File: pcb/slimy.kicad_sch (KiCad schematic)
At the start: 3 parts, among them U1 Teensy3.2, U2 PIM447

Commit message: WIP keyboard pcb design
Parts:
- removed U3: (no value), symbol my_lib:ST7789_240x240
- added D1, D10, D11, D12, D13, D14, D15, D16, D17, D18, D19, D2, D20, D21, D22, D23, D24, D25, D26, D27, D28, D29, D3, D30, D31, D32, D33, D34, D35, D36, D37, D38, D39, D4, D40, D41, D42, D43, D44, D45, D46, D47, D48, D49, D5, D50, D51, D52, D53, D54, D6, D7, D8, D9: D, my_lib:D_SOD123_axial, symbol kicad_lib_tmk:D
- added K1, K10, K11, K12, K13, K14, K15, K16, K17, K18, K19, K2, K20, K21, K22, K23, K24, K25, K26, K27, K28, K29, K3, K30, K31, K32, K33, K34, K35, K36, K37, K38, K39, K4, K40, K41, K42, K43, K44, K45, K46, K47, K48, K49, K5, K50, K51, K52, K53, K54, K6, K7, K8, K9: KEYSW, my_lib:MX-1U-Hotswap-Antishear, symbol kicad_lib_tmk:KEYSW
- added U3: ST7789_SPI, my_lib:ST7789_1.3_240x240, symbol my_lib:ST7789_SPI
- U1: renamed from U2; footprint (none) -> my_lib:PIM447
- U2: renamed from U1; footprint (none) -> teensy:Teensy30_31_32_All_Pins
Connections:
- net GND: now also U3.3 (GND)
- net LCD CS: now also U3.7 (TCS)
- net LCD DC: now also U3.9 (D/C)
- net LCD RST: now also U3.8 (RST)
- net VCC: now also U3.1 (Vin)
- net Col5: now reaches U2.10 (8_TX3_DIN)
- net Col5: now also K17.1, K29.1, K41.1, K5.1, K50.1
- net LCD LITE: now reaches U2.11 (9_RX2_CS_PWM)
- net LCD LITE: now also U3.11 (Lite)
- net Row4: now reaches U2.2 (0_RX1_Touch)
- net Row4: now also D37.1, D38.1, D39.1, D40.1, D41.1, D42.1, D43.1, D44.1, D45.1, D46.1, D47.1, D48.1
- net Row5: now reaches U2.21 (14_A0_SCK)
- net Row5: now also D49.1, D50.1, D51.1, D52.1, D53.1, D54.1, U3.4 (SCK)
- net Col12: now reaches U2.24 (17_A3_SDA0_Touch)
- net Col12: now also K12.1, K24.1, K36.1, K48.1
- net Col11: now reaches U2.27 (20_A6_CS_PWM)
- net Col11: now also K11.1, K23.1, K35.1, K47.1
- net Col10: now reaches U2.28 (21_A7_RX1_CS_PWM)
- net Col10: now also K10.1, K22.1, K34.1, K46.1
- net Col9: now reaches U2.29 (22_A8_Touch_PWM)
- net Col9: now also K21.1, K33.1, K45.1, K54.1, K9.1
- net Row3: now reaches U2.3 (1_TX1_Touch)
- net Row3: now also D25.1, D26.1, D27.1, D28.1, D29.1, D30.1, D31.1, D32.1, D33.1, D34.1, D35.1, D36.1
- net Col8: now reaches U2.30 (23_A9_Touch_PWM)
- net Col8: now also K20.1, K32.1, K44.1, K53.1, K8.1
- net Row2: now reaches U2.4 (2)
- net Row2: now also D13.1, D14.1, D15.1, D16.1, D17.1, D18.1, D19.1, D20.1, D21.1, D22.1, D23.1, D24.1
- net Row1: now reaches U2.5 (3_TX_PWM)
- net Row1: now also D1.1, D10.1, D11.1, D12.1, D2.1, D3.1, D4.1, D5.1, D6.1, D7.1, D8.1, D9.1
- net Col1: now reaches U2.6 (4_RX_PWM)
- net Col1: now also K1.1, K13.1, K25.1, K37.1
- net Col2: now reaches U2.7 (5_TX1_PWM)
- net Col2: now also K14.1, K2.1, K26.1, K38.1
- net Col3: now reaches U2.8 (6_PWM)
- net Col3: now also K15.1, K27.1, K3.1, K39.1
- net Col4: now reaches U2.9 (7_RX3_DOUT)
- net Col4: now also K16.1, K28.1, K4.1, K40.1, K49.1
- net MISO renamed Col7
- net Col7: now also K19.1, K31.1, K43.1, K52.1, K7.1
- net MOSI renamed Col6
- net Col6: now also K18.1, K30.1, K42.1, K51.1, K6.1, U3.6 (SI)
- net SCK: no longer names the net of U2.19 (A14/DAC)
- new net: D16.2, K16.2
- new net: D44.2, K44.2
- new net: D33.2, K33.2
- new net: D17.2, K17.2
- new net: D42.2, K42.2
- new net: D36.2, K36.2
- new net: D11.2, K11.2
- new net: D41.2, K41.2
- new net: D5.2, K5.2
- new net: D6.2, K6.2
- new net: D15.2, K15.2
- new net: D48.2, K48.2
- new net: D28.2, K28.2
- new net: D46.2, K46.2
- new net: D34.2, K34.2
- new net: D21.2, K21.2
- new net: D24.2, K24.2
- new net: D31.2, K31.2
- new net: D40.2, K40.2
- new net: D20.2, K20.2
- new net: D12.2, K12.2
- new net: D29.2, K29.2
- new net: D2.2, K2.2
- new net: D18.2, K18.2
- new net: D4.2, K4.2
- new net: D49.2, K49.2
- new net: D43.2, K43.2
- new net: D37.2, K37.2
- new net: D7.2, K7.2
- new net: D8.2, K8.2
- new net: D9.2, K9.2
- new net: D10.2, K10.2
- new net: D54.2, K54.2
- new net: D32.2, K32.2
- new net: D52.2, K52.2
- new net: D38.2, K38.2
- new net: D13.2, K13.2
- new net: D25.2, K25.2
- new net: D53.2, K53.2
- new net: D22.2, K22.2
- new net: D26.2, K26.2
- new net: D23.2, K23.2
- new net: D50.2, K50.2
- new net: D30.2, K30.2
- new net: D27.2, K27.2
- new net: D19.2, K19.2
- new net: D1.2, K1.2
- new net: D14.2, K14.2
- new net: D39.2, K39.2
- new net: D35.2, K35.2
- new net: D45.2, K45.2
- new net: D3.2, K3.2
- new net: D47.2, K47.2
- new net: D51.2, K51.2
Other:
- moved on the sheet: U1, U2

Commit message: First iteration design pt2
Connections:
- net Col1: no longer U2.6 (4_RX_PWM)
- net Col6: now also U2.6 (4_RX_PWM); no longer U2.13 (11_DOUT), U3.6 (SI)
- net Row1: now also U2.2 (0_RX1_Touch); no longer U2.5 (3_TX_PWM)
- net Row2: now also U2.3 (1_TX1_Touch); no longer U2.4 (2)
- net Row3: now also U2.4 (2); no longer U2.3 (1_TX1_Touch)
- net Row4: now also U2.5 (3_TX_PWM); no longer U2.2 (0_RX1_Touch)
- new net Col_: U2.13 (11_DOUT), U3.6 (SI)
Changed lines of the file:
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@@
     )
   )
-  (global_label "Row2" (shape input) (at 35.56 214.63 180) (fields_autoplaced)
+  (global_label "Row3" (shape input) (at 35.56 214.63 180) (fields_autoplaced)
     (effects (font (size 1.27 1.27)) (justify right))
     (property "Intersheet References" "${INTERSHEET_REFS}" (id 0) (at 28.1879 214.5506 0)
@@
     )
   )
-  (global_label "Row1" (shape input) (at 35.56 217.17 180) (fields_autoplaced)
+  (global_label "Row4" (shape input) (at 35.56 217.17 180) (fields_autoplaced)
     (effects (font (size 1.27 1.27)) (justify right))
     (property "Intersheet References" "${INTERSHEET_REFS}" (id 0) (at 28.1879 217.0906 0)
@@
     )
   )
-  (global_label "Row3" (shape input) (at 35.56 212.09 180) (fields_autoplaced)
+  (global_label "Row2" (shape input) (at 35.56 212.09 180) (fields_autoplaced)
     (effects (font (size 1.27 1.27)) (justify right))
     (property "Intersheet References" "${INTERSHEET_REFS}" (id 0) (at 28.1879 212.0106 0)
@@
     )
   )
-  (global_label "Col6" (shape input) (at 26.67 240.03 180) (fields_autoplaced)
-    (effects (font (size 1.27 1.27)) (justify right))
-    (property "Intersheet References" "${INTERSHEET_REFS}" (id 0) (at 19.9631 240.1094 0)
+  (global_label "Col_" (shape input) (at 26.67 240.03 180) (fields_autoplaced)
+    (effects (font (size 1.27 1.27)) (justify right))
+    (property "Intersheet References" "${INTERSHEET_REFS}" (id 0) (at 20.205 239.9506 0)
       (effects (font (size 1.27 1.27)) (justify right) hide)
     )
@@
     )
   )
-  (global_label "Col1" (shape input) (at 35.56 219.71 180) (fields_autoplaced)
+  (global_label "Col6" (shape input) (at 35.56 219.71 180) (fields_autoplaced)
     (effects (font (size 1.27 1.27)) (justify right))
     (property "Intersheet References" "${INTERSHEET_REFS}" (id 0) (at 28.8531 219.6306 0)
@@
     )
   )
-  (global_label "Row4" (shape input) (at 35.56 209.55 180) (fields_autoplaced)
+  (global_label "Row1" (shape input) (at 35.56 209.55 180) (fields_autoplaced)
     (effects (font (size 1.27 1.27)) (justify right))
     (property "Intersheet References" "${INTERSHEET_REFS}" (id 0) (at 28.1879 209.4706 0)

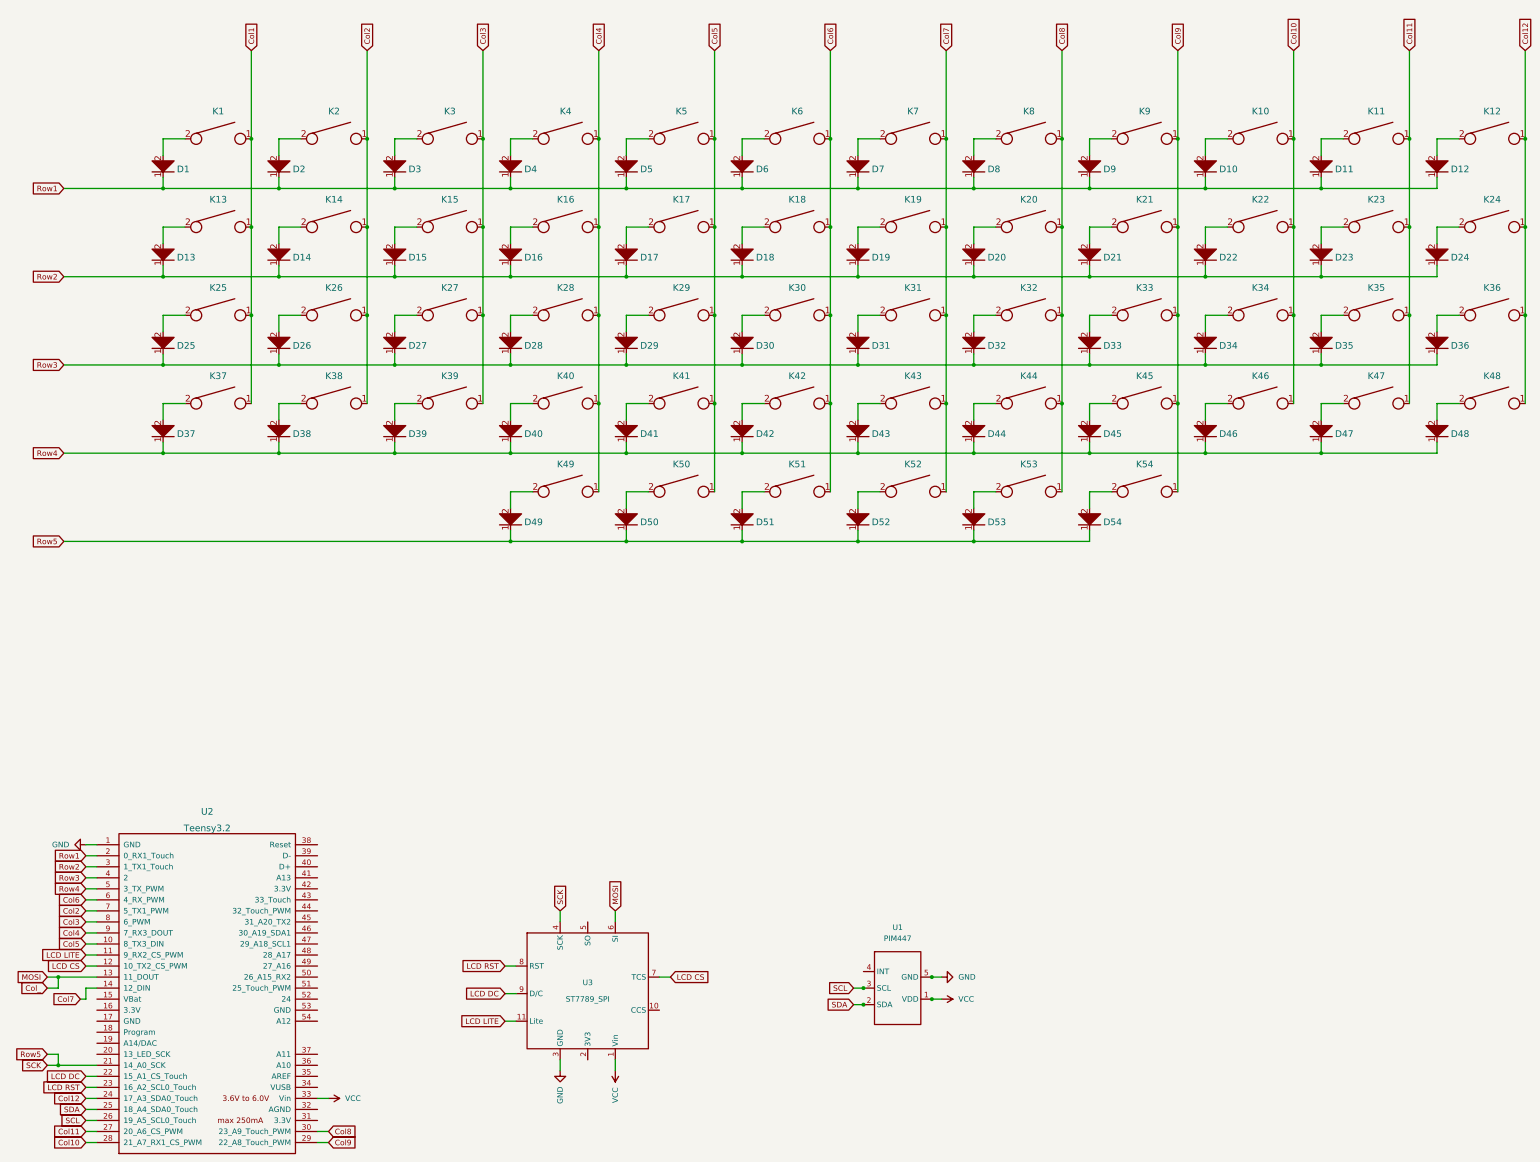
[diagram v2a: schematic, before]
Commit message: Wire everything switch related
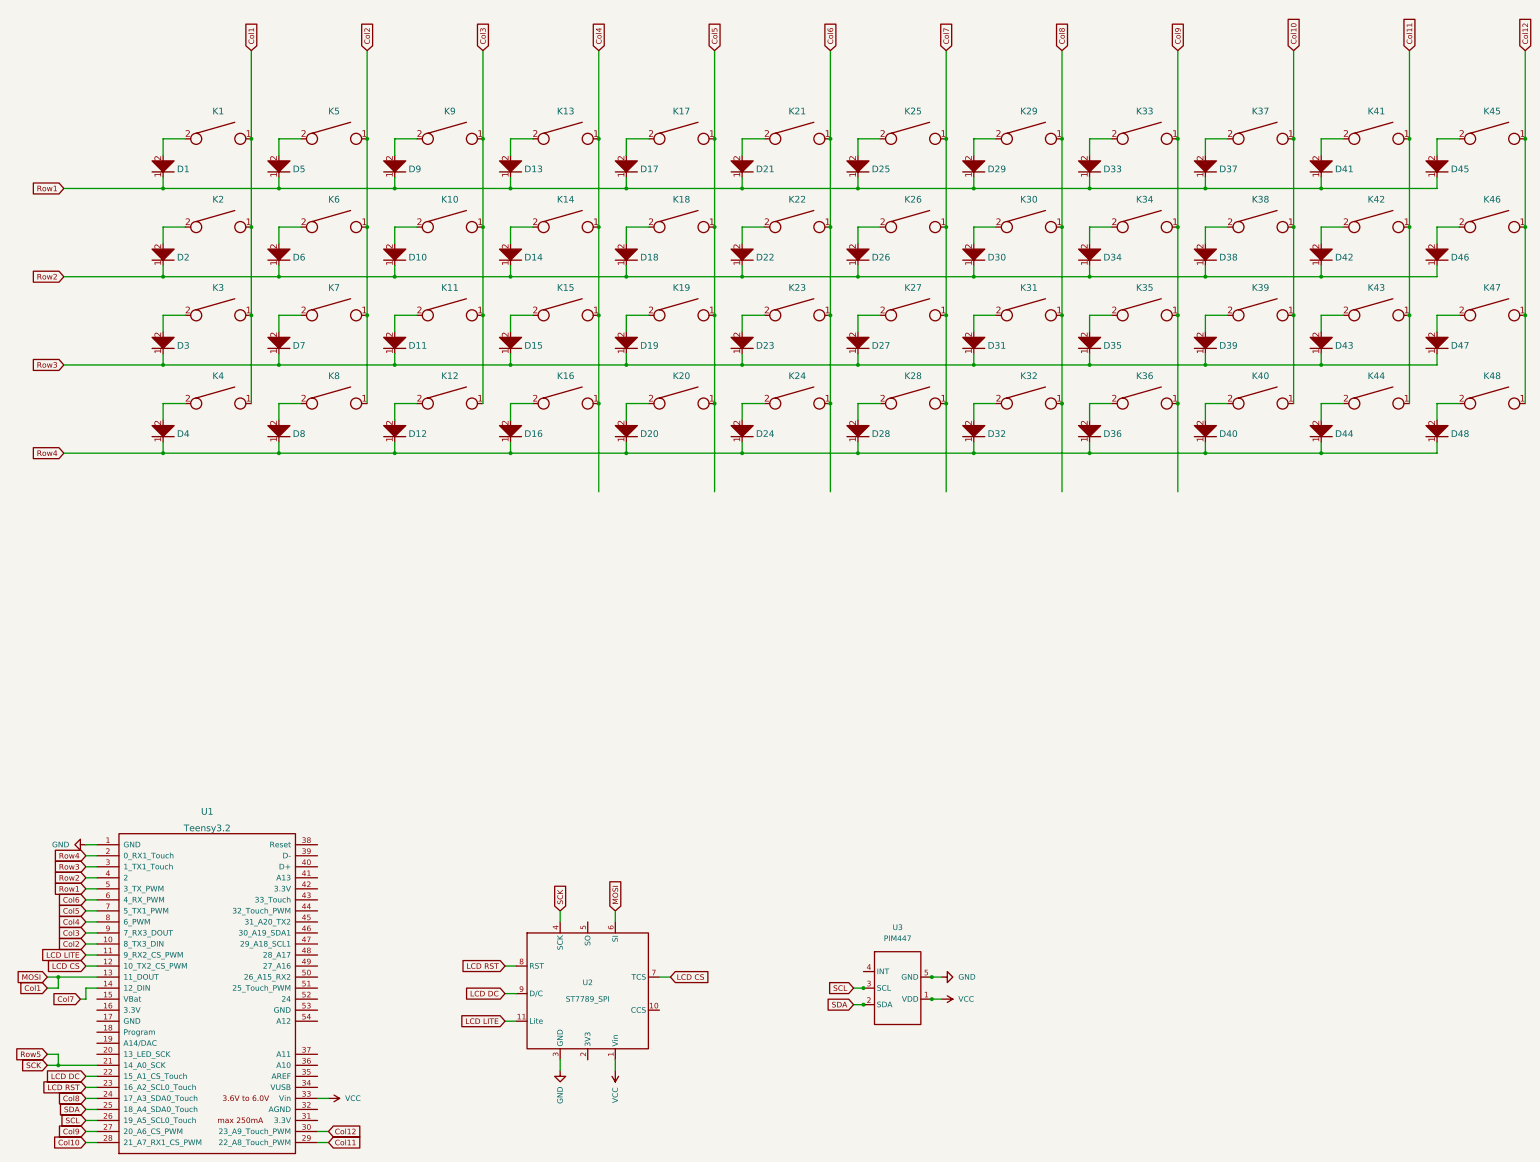
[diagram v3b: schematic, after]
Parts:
- removed D49, D50, D51, D52, D53, D54: D, my_lib:D_SOD123_axial, symbol kicad_lib_tmk:D
- removed K49, K50, K51, K52, K53, K54: KEYSW, my_lib:MX-1U-Hotswap-Antishear, symbol kicad_lib_tmk:KEYSW
- K1, K48: footprint my_lib:MX-1U-Hotswap-Antishear -> (none)
- K10: renamed from K15; footprint my_lib:MX-1U-Hotswap-Antishear -> (none)
- K11: renamed from K27; footprint my_lib:MX-1U-Hotswap-Antishear -> (none)
- K12: renamed from K39; footprint my_lib:MX-1U-Hotswap-Antishear -> (none)
- K13: renamed from K4; footprint my_lib:MX-1U-Hotswap-Antishear -> (none)
- K14: renamed from K16; footprint my_lib:MX-1U-Hotswap-Antishear -> (none)
- K15: renamed from K28; footprint my_lib:MX-1U-Hotswap-Antishear -> (none)
- K16: renamed from K40; footprint my_lib:MX-1U-Hotswap-Antishear -> (none)
- K17: renamed from K5; footprint my_lib:MX-1U-Hotswap-Antishear -> (none)
- K18: renamed from K17; footprint my_lib:MX-1U-Hotswap-Antishear -> (none)
- K19: renamed from K29; footprint my_lib:MX-1U-Hotswap-Antishear -> (none)
- K2: renamed from K13; footprint my_lib:MX-1U-Hotswap-Antishear -> (none)
- K20: renamed from K41; footprint my_lib:MX-1U-Hotswap-Antishear -> (none)
- K21: renamed from K6; footprint my_lib:MX-1U-Hotswap-Antishear -> (none)
- K22: renamed from K18; footprint my_lib:MX-1U-Hotswap-Antishear -> (none)
- K23: renamed from K30; footprint my_lib:MX-1U-Hotswap-Antishear -> (none)
- K24: renamed from K42; footprint my_lib:MX-1U-Hotswap-Antishear -> (none)
- K25: renamed from K7; footprint my_lib:MX-1U-Hotswap-Antishear -> (none)
- K26: renamed from K19; footprint my_lib:MX-1U-Hotswap-Antishear -> (none)
- K27: renamed from K31; footprint my_lib:MX-1U-Hotswap-Antishear -> (none)
- K28: renamed from K43; footprint my_lib:MX-1U-Hotswap-Antishear -> (none)
- K29: renamed from K8; footprint my_lib:MX-1U-Hotswap-Antishear -> (none)
- K3: renamed from K25; footprint my_lib:MX-1U-Hotswap-Antishear -> (none)
- K30: renamed from K20; footprint my_lib:MX-1U-Hotswap-Antishear -> (none)
- K31: renamed from K32; footprint my_lib:MX-1U-Hotswap-Antishear -> (none)
- K32: renamed from K44; footprint my_lib:MX-1U-Hotswap-Antishear -> (none)
- K33: renamed from K9; footprint my_lib:MX-1U-Hotswap-Antishear -> (none)
- K34: renamed from K21; footprint my_lib:MX-1U-Hotswap-Antishear -> (none)
- K35: renamed from K33; footprint my_lib:MX-1U-Hotswap-Antishear -> (none)
- K36: renamed from K45; footprint my_lib:MX-1U-Hotswap-Antishear -> (none)
- K37: renamed from K10; footprint my_lib:MX-1U-Hotswap-Antishear -> (none)
- K38: renamed from K22; footprint my_lib:MX-1U-Hotswap-Antishear -> (none)
- K39: renamed from K34; footprint my_lib:MX-1U-Hotswap-Antishear -> (none)
- K4: renamed from K37; footprint my_lib:MX-1U-Hotswap-Antishear -> (none)
- K40: renamed from K46; footprint my_lib:MX-1U-Hotswap-Antishear -> (none)
- K41: renamed from K11; footprint my_lib:MX-1U-Hotswap-Antishear -> (none)
- K42: renamed from K23; footprint my_lib:MX-1U-Hotswap-Antishear -> (none)
- K43: renamed from K35; footprint my_lib:MX-1U-Hotswap-Antishear -> (none)
- K44: renamed from K47; footprint my_lib:MX-1U-Hotswap-Antishear -> (none)
- K45: renamed from K12; footprint my_lib:MX-1U-Hotswap-Antishear -> (none)
- K46: renamed from K24; footprint my_lib:MX-1U-Hotswap-Antishear -> (none)
- K47: renamed from K36; footprint my_lib:MX-1U-Hotswap-Antishear -> (none)
- K5: renamed from K2; footprint my_lib:MX-1U-Hotswap-Antishear -> (none)
- K6: renamed from K14; footprint my_lib:MX-1U-Hotswap-Antishear -> (none)
- K7: renamed from K26; footprint my_lib:MX-1U-Hotswap-Antishear -> (none)
- K8: renamed from K38; footprint my_lib:MX-1U-Hotswap-Antishear -> (none)
- K9: renamed from K3; footprint my_lib:MX-1U-Hotswap-Antishear -> (none)
- renumbered D15 to D10, D27 to D11, D39 to D12, D4 to D13, D16 to D14, D28 to D15, D40 to D16, D5 to D17, D17 to D18, D29 to D19, D13 to D2, D41 to D20, D6 to D21, D18 to D22, D30 to D23, D42 to D24, D7 to D25, D19 to D26, D31 to D27, D43 to D28, D8 to D29, D25 to D3, D20 to D30, D32 to D31, D44 to D32, D9 to D33, D21 to D34, D33 to D35, D45 to D36, D10 to D37, D22 to D38, D34 to D39, D37 to D4, D46 to D40, D11 to D41, D23 to D42, D35 to D43, D47 to D44, D12 to D45, D24 to D46, D36 to D47, D2 to D5, D14 to D6, D26 to D7, D38 to D8, D3 to D9, U2 to U1, U3 to U2, U1 to U3
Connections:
- net Col_ is gone; now on net Col1: U1.13 (11_DOUT), U2.6 (SI)
- net Col11: now also U1.29 (22_A8_Touch_PWM); no longer U1.27 (20_A6_CS_PWM)
- net Col12: now also U1.30 (23_A9_Touch_PWM); no longer U1.24 (17_A3_SDA0_Touch)
- net Col2: now also U1.10 (8_TX3_DIN); no longer U1.7 (5_TX1_PWM)
- net Col3: now also U1.9 (7_RX3_DOUT); no longer U1.8 (6_PWM)
- net Col4: now also U1.8 (6_PWM); no longer U1.9 (7_RX3_DOUT)
- net Col5: now also U1.7 (5_TX1_PWM); no longer U1.10 (8_TX3_DIN)
- net Col8: now also U1.24 (17_A3_SDA0_Touch); no longer U1.30 (23_A9_Touch_PWM)
- net Col9: now also U1.27 (20_A6_CS_PWM); no longer U1.29 (22_A8_Touch_PWM)
- net Row1: now also U1.5 (3_TX_PWM); no longer U1.2 (0_RX1_Touch)
- net Row2: now also U1.4 (2); no longer U1.3 (1_TX1_Touch)
- net Row3: now also U1.3 (1_TX1_Touch); no longer U1.4 (2)
- net Row4: now also U1.2 (0_RX1_Touch); no longer U1.5 (3_TX_PWM)
